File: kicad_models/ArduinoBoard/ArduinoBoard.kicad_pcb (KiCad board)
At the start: 2 copper layers, 6 parts, among them J1 5V Output, J2 Buttons, J3 PWM Output, J4 Screw_Terminal_01x02, J5 Conn_01x04_Pin

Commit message: Updated the KiCad files.
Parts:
- added J6: OLED, Connector_PinHeader_2.54mm:PinHeader_1x04_P2.54mm_Vertical, F.Cu at (113.1, 107.0)
- moved J5 46.8 mm to (132.5, 105.0)
- moved J3 39.7 mm to (132.0, 57.2), turned to -90 degrees
- moved A1 26.1 mm to (120.7, 96.1), turned to 180 degrees
- moved J2 23.3 mm to (132.0, 69.0), turned to -90 degrees
- moved J4 21.9 mm to (132.0, 92.0), turned to -90 degrees
- moved J1 21.4 mm to (132.0, 80.5), turned to -90 degrees
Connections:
- A1 pad 23: unconnected-(A1-A4-Pad23) -> Net-(A1-A4)
- A1 pad 24: unconnected-(A1-A5-Pad24) -> Net-(A1-A5)
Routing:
- net Net-(A1-+5V): track 0.00 -> 109.5 mm
- net Net-(J1-Pin_1): track 0.00 -> 84.5 mm
- net Net-(J4-Pin_2): track 0.00 -> 45.4 mm
- net Net-(A1-VIN): track 0.00 -> 33.9 mm
- net Net-(A1-A4): track 0.00 -> 32.8 mm
- net Net-(A1-A5): track 0.00 -> 30.1 mm
- net Net-(A1-D3): track 0.00 -> 22.5 mm
- net Net-(A1-D2): track 0.00 -> 20.3 mm
- net Net-(J4-Pin_1): track 0.00 -> 19.7 mm
- net Net-(A1-D11): track 0.00 -> 14.0 mm
- net Net-(A1-D10): track 0.00 -> 12.7 mm

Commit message: Updated the PCB file I was working on.
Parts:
- added H1: MountingHole, MountingHole:MountingHole_2.2mm_M2_DIN965_Pad, F.Cu at (102.5, 52.5)
- added H2: MountingHole, MountingHole:MountingHole_2.2mm_M2_DIN965_Pad, F.Cu at (138.5, 52.5)
- added H3: MountingHole, MountingHole:MountingHole_2.2mm_M2_DIN965_Pad, F.Cu at (138.5, 118.5)
- added H4: MountingHole, MountingHole:MountingHole_2.2mm_M2_DIN965_Pad, F.Cu at (102.5, 118.5)
- moved J6 15.9 mm to (124.0, 118.5)
- moved A1 0.61 mm to (121.1, 96.5)
- moved J3 0.25 mm to (132.0, 57.5)
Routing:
- net Net-(A1-A5): track 30.1 -> 52.8 mm
- net Net-(A1-A4): track 32.8 -> 54.7 mm
- net Net-(A1-+5V): track 109.5 -> 95.9 mm
- net Net-(J1-Pin_1): track 84.5 -> 71.2 mm
- net Net-(J4-Pin_2): track 45.4 -> 44.8 mm
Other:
- board outline added: 40 x 70 mm
- board text added: "+12V"
- board text added: "+5V"
- board text added: "12V Input"
- board text added: "5V Output"
- board text added: "Arduino Nano"
- board text added: "Extend"
- board text added: "GND"
- board text added: "Motor Driver PWM"
- board text added: "Retract"
- board text added: "Switch/Buttons"

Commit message: Updated the kicad files some more
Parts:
- J1, J2, J3, J4: footprint TerminalBlock:TerminalBlock_MaiXu_MX126-5.0-02P_1x02_P5.00mm -> TerminalBlock:TerminalBlock_bornier-2_P5.08mm
- moved J5 24.5 mm to (108.0, 105.0)
- moved J4 2.80 mm to (132.0, 89.2)
- moved J1 1.40 mm to (132.0, 79.1)
- moved J3 1.36 mm to (132.0, 58.9)
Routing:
- net Net-(J4-Pin_1): track 20.1 -> 47.8 mm
- net Net-(A1-VIN): track 33.9 -> 20.5 mm
- net Net-(J4-Pin_2): track 44.8 -> 53.6 mm
- net Net-(A1-+5V): track 95.9 -> 93.2 mm
- net Net-(J1-Pin_1): track 71.2 -> 68.7 mm
- net Net-(A1-D10): track 12.5 -> 11.8 mm
- net Net-(A1-D11): track 13.8 -> 13.1 mm
- net Net-(A1-A4): track 54.7 -> 55.3 mm
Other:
- board text added: "Buck Converter 9V Out"

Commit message: Updated PCB file again.
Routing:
- net Net-(J4-Pin_2): track 53.6 -> 52.3 mm
- net Net-(J1-Pin_1): track 68.7 -> 69.7 mm
- net Net-(A1-+5V): track 93.2 -> 92.7 mm
- net Net-(A1-D2): track 20.1 -> 20.6 mm

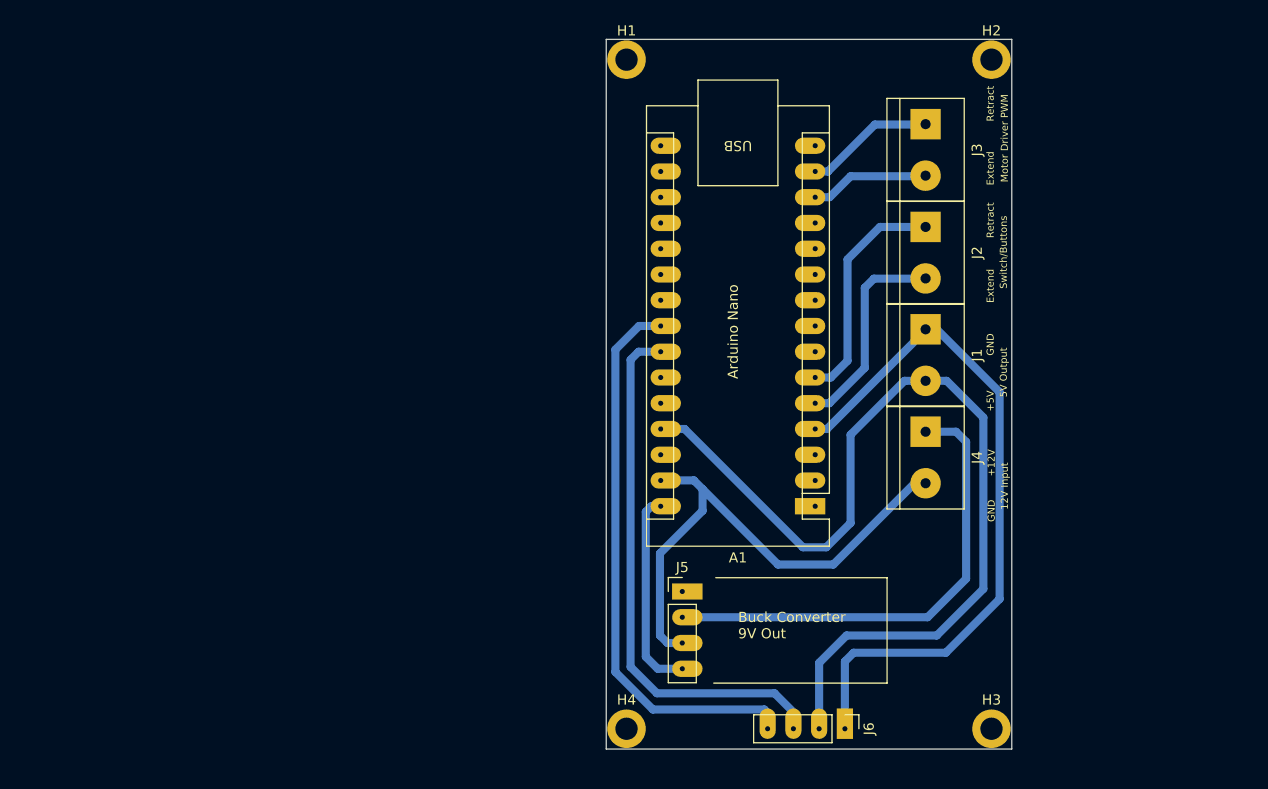
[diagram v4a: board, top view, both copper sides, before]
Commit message: Had to make some updates after my first prototype PCB. Hopefully this version is correct. :)
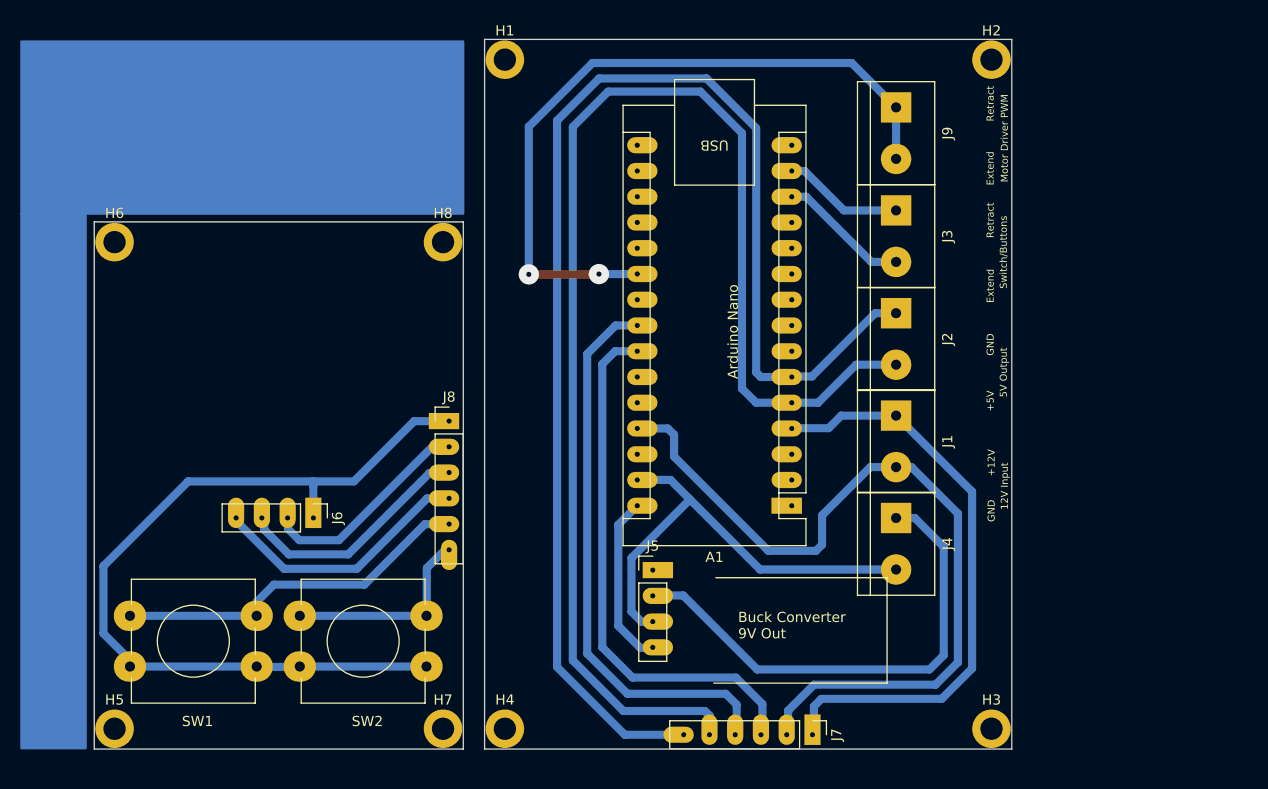
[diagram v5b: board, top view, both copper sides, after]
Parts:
- added H5: MountingHole, MountingHole:MountingHole_2.2mm_M2_DIN965_Pad, F.Cu at (52.0, 118.5)
- added H6: MountingHole, MountingHole:MountingHole_2.2mm_M2_DIN965_Pad, F.Cu at (52.0, 70.5)
- added H7: MountingHole, MountingHole:MountingHole_2.2mm_M2_DIN965_Pad, F.Cu at (84.4, 118.5)
- added H8: MountingHole, MountingHole:MountingHole_2.2mm_M2_DIN965_Pad, F.Cu at (84.4, 70.5)
- added J7: Conn_01x06_Pin, Connector_PinHeader_2.54mm:PinHeader_1x06_P2.54mm_Vertical, F.Cu at (120.8, 119.1)
- added J8: Conn_01x06_Pin, Connector_PinHeader_2.54mm:PinHeader_1x06_P2.54mm_Vertical, F.Cu at (85.0, 88.2)
- added J9: Position Input, TerminalBlock:TerminalBlock_bornier-2_P5.08mm, F.Cu at (129.1, 57.2)
- added SW1: SW_Push_Dual, Button_Switch_THT:SW_PUSH-12mm, F.Cu at (66.0, 112.4)
- added SW2: SW_Push_Dual, Button_Switch_THT:SW_PUSH-12mm, F.Cu at (82.8, 112.4)
- J4: value Screw_Terminal_01x02 -> 12V Input
- J6: value OLED -> Conn_01x04_Pin
- moved J6 56.4 mm to (71.6, 97.7)
- moved H1 12.0 mm to (90.5, 52.5)
- moved H4 12.0 mm to (90.5, 118.5)
- moved J1 8.99 mm to (129.1, 87.6)
- moved J2 8.99 mm to (129.1, 77.5)
- moved J3 8.99 mm to (129.1, 67.4)
- moved J4 8.99 mm to (129.1, 97.7)
- moved J5 3.59 mm to (105.1, 102.8)
- moved A1 2.31 mm to (118.8, 96.5)
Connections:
- A1 pad 21: unconnected-(A1-A2-Pad21) -> Net-(A1-A2)
- J6 pad 1: Net-(J1-Pin_1) -> Net-(J6-Pin_1)
- J6 pad 2: Net-(A1-+5V) -> Net-(J6-Pin_2)
- J6 pad 3: Net-(A1-A5) -> Net-(J6-Pin_3)
- J6 pad 4: Net-(A1-A4) -> Net-(J6-Pin_4)
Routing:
- net Net-(A1-D2): track 20.6 -> 133.1 mm
- net Net-(A1-D3): track 22.9 -> 133.4 mm
- net Net-(J6-Pin_1): track 0.00 -> 83.1 mm
- net Net-(A1-A2): track 0.00 -> 71.0 mm, vias 0 -> 2
- net Net-(J8-Pin_5): track 0.00 -> 35.2 mm
- net Net-(J6-Pin_4): track 0.00 -> 28.2 mm
- net Net-(J6-Pin_3): track 0.00 -> 25.7 mm
- net Net-(J6-Pin_2): track 0.00 -> 23.3 mm
- net Net-(J8-Pin_6): track 0.00 -> 19.1 mm
- net Net-(A1-+5V): track 92.7 -> 80.3 mm
- net Net-(J1-Pin_1): track 69.7 -> 58.4 mm
- net Net-(J4-Pin_2): track 52.3 -> 45.8 mm
- net Net-(A1-VIN): track 20.1 -> 17.0 mm
- net Net-(J4-Pin_1): track 48.3 -> 49.5 mm
- net Net-(A1-D10): track 11.8 -> 13.0 mm
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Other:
- board size 40 x 70 mm -> 90.5 x 70 mm
- board text added: "12V+ IN"
- board text added: "5V+ OUT"
- board text added: "90 deg male pins"
- board text added: "Ext Ret BUTTONS"
- board text added: "Ext Ret PWM"
- board text added: "OLED Screen"
- board text added: "SW1"
- board text added: "SW2"
- board text added: "Sensor Input Use Either"
- board text added: "USB"

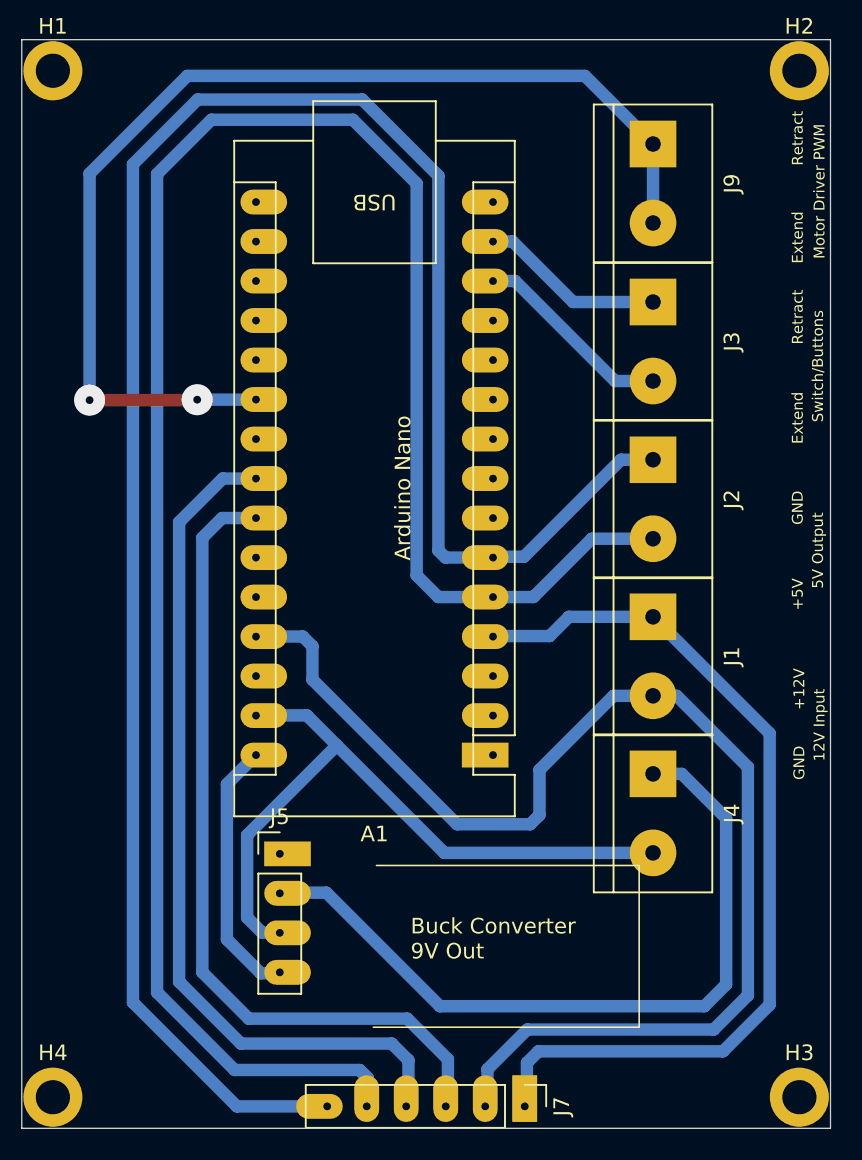
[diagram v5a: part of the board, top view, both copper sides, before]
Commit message: Added a 0.1uF capacitor and linked the two GND pins on the Arduino. I seem to have overloaded the Arduino when I plugged in the 12V input - probably a surge. The capacitor should condition the circuit momentarily.
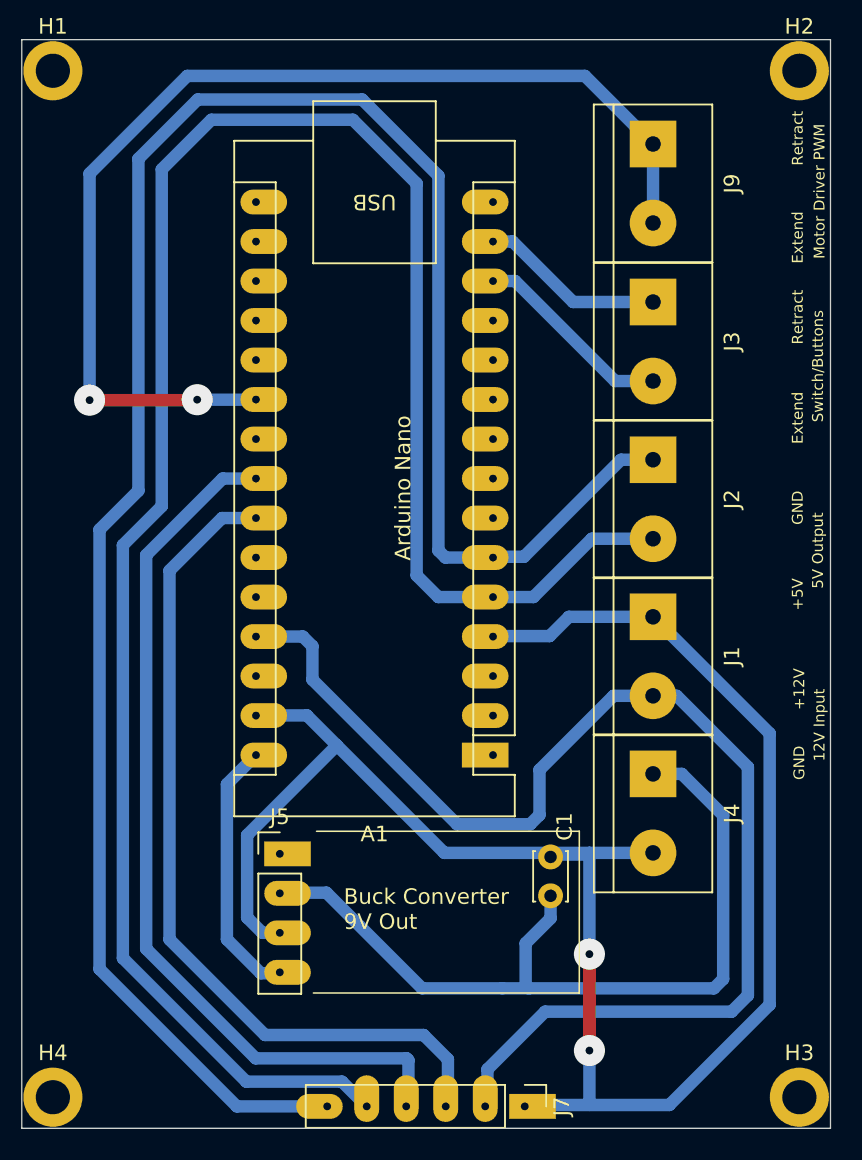
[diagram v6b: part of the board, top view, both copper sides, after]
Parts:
- added C1: 0.1uF, Capacitor_THT:C_Disc_D3.0mm_W2.0mm_P2.50mm, F.Cu at (122.5, 103.0)
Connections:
- A1 pad 29: Net-(J4-Pin_2) -> Net-(J1-Pin_1)
- J4 pad 2: Net-(J4-Pin_2) -> Net-(J1-Pin_1)
- J5 pad 3: Net-(J4-Pin_2) -> Net-(J1-Pin_1)
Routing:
- net Net-(J1-Pin_1): track 58.4 -> 121.9 mm, vias 0 -> 2
- net Net-(J4-Pin_2): track 45.8 -> 0.00 mm
- net Net-(J4-Pin_1): track 49.5 -> 54.8 mm
- net Net-(A1-D3): track 133.4 -> 135.1 mm
- net Net-(A1-A4): track 55.0 -> 56.8 mm
- net Net-(A1-A5): track 52.6 -> 54.4 mm
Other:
- board text added: "C1 0.1uF"

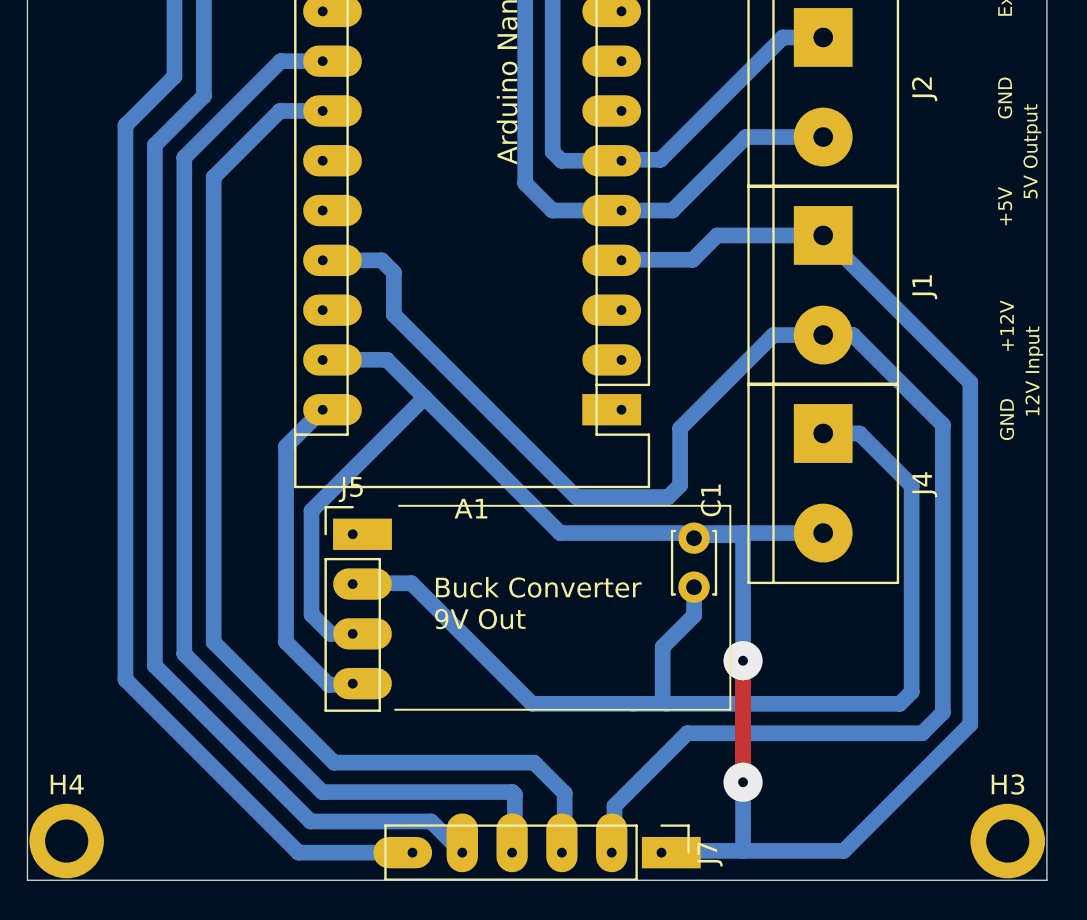
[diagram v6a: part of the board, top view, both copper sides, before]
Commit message: Learned that adding a capacitor could actually make the surge worse. Changed to a Negative Temperature Coeficient (NTC) Thermistor instead. The thermistor adds resistance when cool and heats up with use, softening the surge to the buck converter.
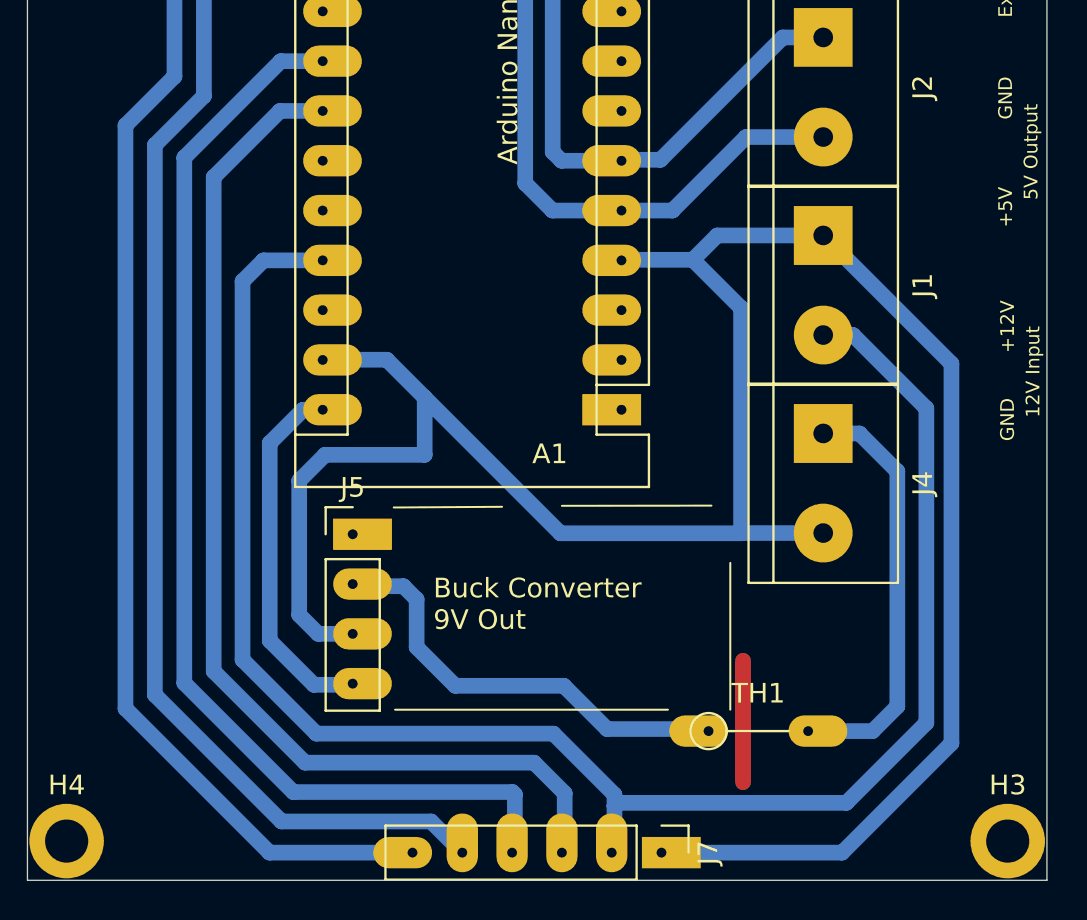
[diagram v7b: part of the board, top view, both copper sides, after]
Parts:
- removed C1: 0.1uF, Capacitor_THT:C_Disc_D3.0mm_W2.0mm_P2.50mm
- added TH1: Thermistor_NTC, Resistor_THT:R_Axial_DIN0204_L3.6mm_D1.6mm_P5.08mm_Vertical, F.Cu at (123.2, 112.9)
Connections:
- J5 pad 2: Net-(J4-Pin_1) -> Net-(J5-Pin_2)
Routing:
- net Net-(J4-Pin_1): track 54.8 -> 21.6 mm
- net Net-(J5-Pin_2): track 0.00 -> 29.8 mm
- net Net-(A1-+5V): track 80.3 -> 88.7 mm
- net Net-(A1-VIN): track 17.0 -> 18.7 mm
- net Net-(A1-D2): track 133.3 -> 134.2 mm
- net Net-(A1-A4): track 56.8 -> 57.7 mm
- net Net-(A1-D3): track 135.1 -> 136.0 mm
- net Net-(A1-A5): track 54.4 -> 55.2 mm
- net Net-(J1-Pin_1): track 121.9 -> 121.1 mm, vias 2 -> 0
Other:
- board text added: "12V Power"
- board text added: "5V Power"
- board text added: "Buttons"
- board text added: "Ext Ret"
- board text added: "PWM"
- board text added: "Pos. Sensor (Use Either)"
- board text added: "TH1 NTC Thermistor"
- board text removed: "12V+ IN"
- board text removed: "5V+ OUT"
- board text removed: "C1 0.1uF"
- board text removed: "Ext Ret BUTTONS"
- board text removed: "Ext Ret PWM"
- board text removed: "Sensor Input Use Either"
